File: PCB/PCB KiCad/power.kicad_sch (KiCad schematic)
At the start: 3 parts

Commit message: Minor schematic cleanup!
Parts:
- added C13: 10u, Capacitor_SMD:C_0805_2012Metric_Pad1.18x1.45mm_HandSolder, symbol Device:C
- added U3: AMS1117-3.3, Package_TO_SOT_SMD:SOT-223-3_TabPin2, symbol Regulator_Linear:AMS1117-3.3
- renumbered C12 to C14, C13 to C15
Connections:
- net 3v3unf: now also U3.2 (VO)
- net GND: now also C13.2, U3.1 (GND)
- net +3V3 renamed +3.3V
- new net 5v_RAW: C13.1, U3.3 (VI)

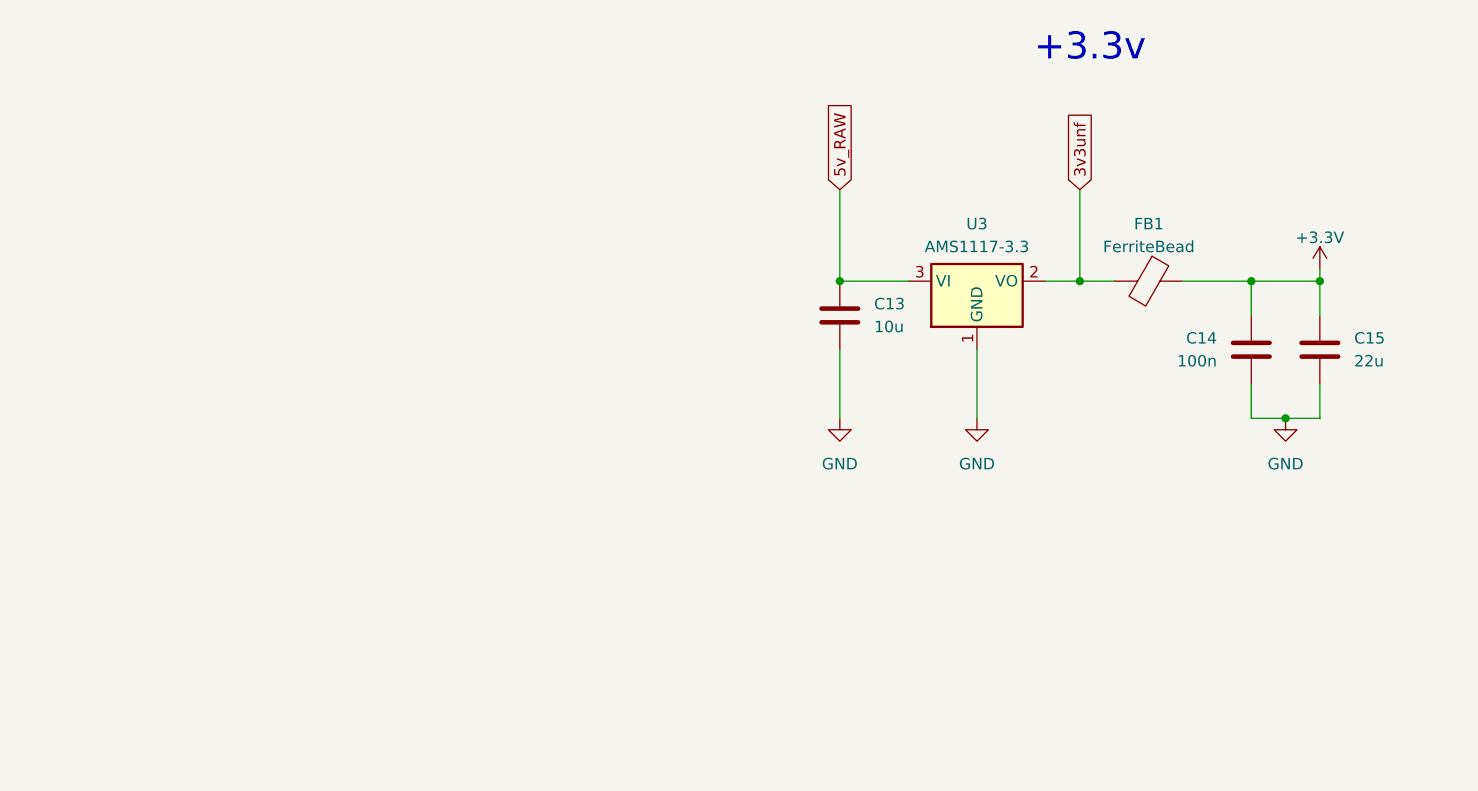
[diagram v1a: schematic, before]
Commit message: Giant schematic cleanup to make more sense of the sensor circuit and just clean everything up a bit.
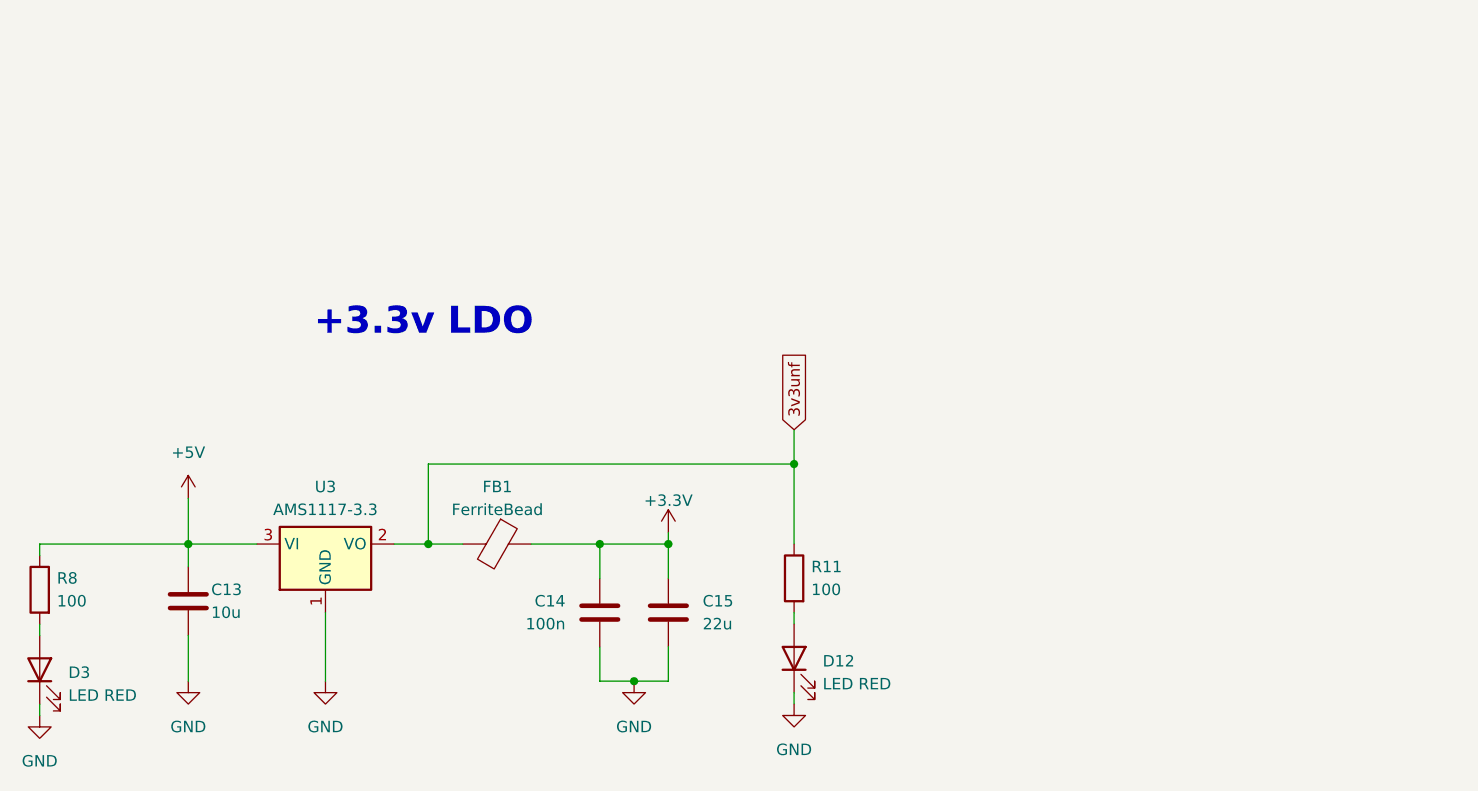
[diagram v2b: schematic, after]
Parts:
- added D12, D3: LED RED, LED_SMD:LED_0805_2012Metric_Pad1.15x1.40mm_HandSolder, symbol Device:LED
- added R11, R8: 100, Resistor_SMD:R_0805_2012Metric_Pad1.20x1.40mm_HandSolder, symbol Device:R
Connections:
- net 3v3unf: now also R11.1
- net GND: now also D12.1 (K), D3.1 (K)
- net 5v_RAW renamed +5V
- net +5V: now also R8.1
- new net: D3.2 (A), R8.2
- new net: D12.2 (A), R11.2
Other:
- note added: "+3.3v LDO"
- note removed: "+3.3v"
- moved on the sheet: C13, C14, C15, FB1, U3
